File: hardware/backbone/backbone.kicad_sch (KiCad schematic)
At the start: 87 parts, among them J10 CORE_A, J11 MOUNT, J13 FIELD_B, J14 FIELD_A, J2 FROM_PREVIOUS, J4 FROM_PREVIOUS, J5 CONN_A, J7 CONN_B, J8 CORE_B, J9 TO NEXT, Q2 AO3401A, U11 470nH DCR=450m, U13 470nH DCR=450m, U15 ST25R100, U17 BLM18PG471SZ1D, U19 ESP32-S3-MINI-1, U2 SN65HVD230DR, U4 AP2112K-3.3TRG1, U8 G3VM-61VY3, X1 NX2016SA 27.12MHz

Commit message: New design, no NFC, added bottom-top side socket, board less expensive
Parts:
- removed ANT1, ANT2: Net-Tie-Width-0.50mm, SpaghettiLAB:ST25Rxxx-ANT-12x12mm, symbol STMICRO:root_1_Net-Tie-Width-0.50mm_STMICRO.SchLib
- removed C13, C16: 200pF 1%, SpaghettiLAB:C0603, symbol STMICRO:root_1_Capacitor 0402 240pF 50V 2% COG_STMICRO.SchLib
- removed C18, C20: 10pF, SpaghettiLAB:C0603, symbol STMICRO:root_1_Capacitor 0201 10pF 25V_STMICRO.SchLib
- removed C23: 100nF, SpaghettiLAB:C0603, symbol STMICRO:root_1_GRM033C71A104KE14D_STMICRO.SchLib
- removed C28, C32: 33pF 2%, SpaghettiLAB:C0603, symbol STMICRO:root_0_Capacitor 0603 39pF 50V 2% COG_STMICRO.SchLib
- removed C30, C35, C37, C58, C63, C65: 10nF, SpaghettiLAB:C0603, symbol STMICRO:root_1_GRM033R61E103KA12D_STMICRO.SchLib
- removed C33, C39, C41, C70: 2.2uF/10V, SpaghettiLAB:C0603, symbol STMICRO:root_1_GRM033R61A225ME47_STMICRO.SchLib
- removed C43, C55: 220pF, SpaghettiLAB:C0603, symbol STMICRO:root_1_Capacitor 0603 220pF 50V C0G 2%_STMICRO.SchLib
- removed C46, C54: 10pF, SpaghettiLAB:C0603, symbol STMICRO:root_1_Capacitor 0603 10pF 25V 5% C0G_STMICRO.SchLib
- removed C48, C51: 150pF, SpaghettiLAB:C0603, symbol STMICRO:root_1_Capacitor 0603 150pF 50V 2% COG_STMICRO.SchLib
- removed C60, C72: 1uF/10V, SpaghettiLAB:C0603, symbol STMICRO:root_1_GRM033R61A105ME15_STMICRO.SchLib
- removed C62: 4.7uF/10V, SpaghettiLAB:C0603, symbol STMICRO:root_1_GRM155R61A475MEAA_STMICRO.SchLib
- removed D2, D3: LED, SpaghettiLAB:LED0603-RD, symbol Device:LED
- removed J10: CORE_A, Connector_PinSocket_2.54mm:PinSocket_1x03_P2.54mm_Vertical, symbol Connector:Conn_01x03_Pin
- removed J11: MOUNT, Connector_PinHeader_2.54mm:PinHeader_1x05_P2.54mm_Horizontal, symbol Connector:Conn_01x05_Pin
- removed J13: FIELD_B, Connector_PinSocket_2.54mm:PinSocket_1x03_P2.54mm_Vertical, symbol Connector:Conn_01x03_Pin
- removed J14: FIELD_A, Connector_PinSocket_2.54mm:PinSocket_1x03_P2.54mm_Vertical, symbol Connector:Conn_01x03_Pin
- removed J4: FROM_PREVIOUS, Connector_PinSocket_2.54mm:PinSocket_1x05_P2.54mm_Horizontal, symbol Connector:Conn_01x05_Socket
- removed J5: CONN_A, Connector_PinSocket_2.54mm:PinSocket_1x03_P2.54mm_Vertical, symbol Connector:Conn_01x03_Pin
- removed J7: CONN_B, Connector_PinSocket_2.54mm:PinSocket_1x03_P2.54mm_Vertical, symbol Connector:Conn_01x03_Pin
- removed J8: CORE_B, Connector_PinSocket_2.54mm:PinSocket_1x03_P2.54mm_Vertical, symbol Connector:Conn_01x03_Pin
- removed L2: 420nH DCR=450m, STMICRO.PcbLib:COILCRAFT-SELF-SERIE-0402DF, symbol STMICRO:root_0_COILCRAFT-SELF-0402DF-421XJR_STMICRO.SchLib
- removed L4: BLM15PD121SN1D, symbol STMICRO:root_0_BLM15PD121SN1D_STMICRO.SchLib
- removed R11, R14: 1R5, SpaghettiLAB:R0603, symbol STMICRO:root_0_Resistor 0603 1R5 1%_STMICRO.SchLib
- removed R21, R22: 330R, SpaghettiLAB:R0603, symbol Device:R
- removed TP17, TP20: SMD/0.8mm, TestPoint:TestPoint_Pad_D1.0mm, symbol STMICRO:root_0_PLAGE-CMS-DIAM-0.8mm_STMICRO.SchLib
- removed TP2, TP4: SMD/0.8mm, TestPoint:TestPoint_Pad_D1.0mm, symbol STMICRO:root_1_PLAGE-CMS-DIAM-0.8mm_STMICRO.SchLib
- removed U11, U13: 470nH DCR=450m, SpaghettiLAB:IND-SMD_L1.6-W0.8-1, symbol SpaghettiLAB:LQW18CNR47J00D
- removed U15: ST25R100, SpaghettiLAB:QFN-24_L4.0-W4.0-P0.50-TL-EP2.8, symbol STMICRO:root_0_ST25R200_STMICRO.SchLib
- removed U17: BLM18PG471SZ1D, SpaghettiLAB:L0603, symbol SpaghettiLAB:BLM18PG471SZ1D
- removed X1: NX2016SA 27.12MHz, SpaghettiLAB:CRYSTAL-SMD_4P-L2.0-W1.6-BL, symbol STMICRO:root_1_NDK-NX2016SA-27.12MHZ-EXS00A-CS01188_STMICRO.SchLib_0
- added H1, H2, H3, H4: MountingHole, MountingHole:MountingHole_2.2mm_M2_DIN965, symbol Mechanical:MountingHole
- added J1, J140, J3: M20-7810645R, SpaghettiLAB:HARWIN_M20-7810645R, symbol SpaghettiLAB:M20-7810645R
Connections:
- net IO11 is gone; now on net STATUS: U19.15 (IO11)
- net IO7 is gone; now on net A0: U19.11 (IO7)
- net IO8 is gone; now on net A1: U19.12 (IO8)
- net IO9 is gone; now on net A2: U19.13 (IO9)
- net 5V: now also J3.2
- net A0: now also J3.6; no longer U19.34 (IO38)
- net A1: now also J3.8; no longer U19.33 (IO37)
- net A2: now also J3.10; no longer U19.32 (IO36)
- net A3: now also U19.14 (IO10), J3.12; no longer U19.31 (IO35)
- net GND: now also J3.3, J3.4
- net STATUS: no longer U19.14 (IO10)
- net VCORE: now also J3.1
- net IO12 renamed A4
- net A4: now also J3.11
- net IO13 renamed A5
- net A5: now also J3.9
- net IO14 renamed A6
- net A6: now also J3.7
- net IO15 renamed A7
- net A7: now also J3.5
- net NFC_CS renamed IO2
- net NFC_IRQ renamed IO5
- net NFC_MISO renamed IO6
- net NFC_MOSI renamed IO3
- net NFC_RST renamed IO1
- net NFC_SCK renamed IO4
- new net: J1.2, J140.1
- new net: J1.9, J140.10
- new net: J1.12, J140.11
- new net: J1.11, J140.12
- new net: J1.1, J140.2
- new net: J1.4, J140.3
- new net: J1.3, J140.4
- new net: J1.6, J140.5
- new net: J1.5, J140.6
- new net: J1.8, J140.7
- new net: J1.7, J140.8
- new net: J1.10, J140.9
- new net IO35: U19.31 (IO35)
- new net IO36: U19.32 (IO36)
- new net IO37: U19.33 (IO37)
- new net IO38: U19.34 (IO38)
- no-connect marks 22 -> 12
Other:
- note removed: "0402 NOT EASY TO FIND/MOUNT SWITCHED TO 0603, A RE-TUNE MAY BE NECESSARY"
- note removed: "0603"
- note removed: "0603 BETTER C0G/NP0"
- note removed: "BLM15PD121SN1D WAS NOT IN INVENTORY BUT IS THE SUGGESTED ONE"
- note removed: "NFC ANTENNA"
- note removed: "NFC ANTENNA PARAMETERS Type: PCB Spiral Coil (Double Layer) Frequency: 13.56 MHz Size: 12 mm x 12 mm Layers: TOP + BOTTOM copper Turns: 6 total (3 TOP + 3 BOTTOM) Connection: Series through vias PCB: Substrate: FR-4 Thickness: 1.6 mm Relative Er: 4.4 Copper thickness: 35 um Geometry: Track width: 0.5 mm Track spacing: 0.5 mm Outer diameter: 12 mm Inner diameter: 6 mm Average diameter: 9 mm Electr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"
- note removed: "NFC MODULE READER 0"
- note removed: "USED 0603 INSTEAD TO MATCH OTHER COMPONENTS OF THE NET"
- note removed: "| ADC | Channels | GPIO | | ADC1 | CH0-CH9 | **GPIO1-GPIO10** | | ADC2 | CH0-CH9 | **GPIO11-GPIO20** | NEXT REVIEW NEEDS THIS MODS"
- moved on the sheet: D5, R24

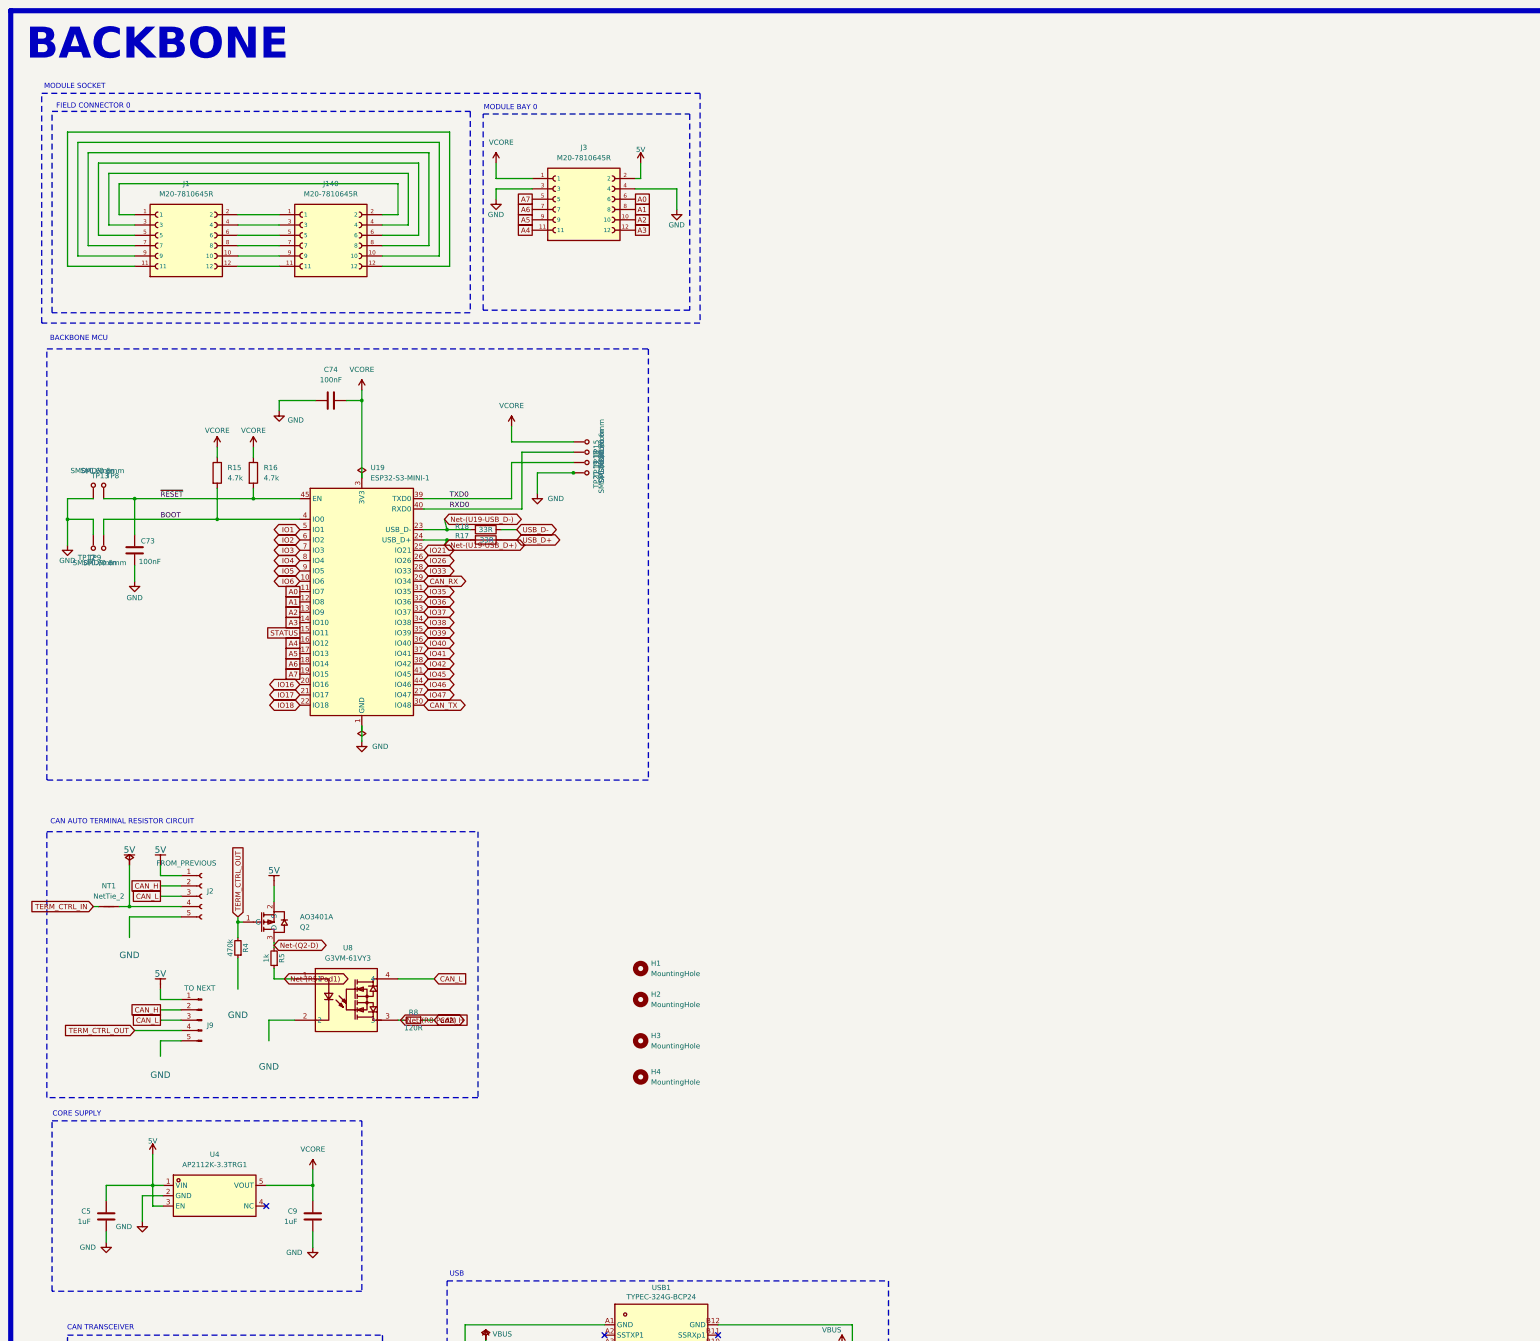
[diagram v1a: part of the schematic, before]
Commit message: Prepare V3 hardware with S3 FlexyPin socket and expansion connector libraries
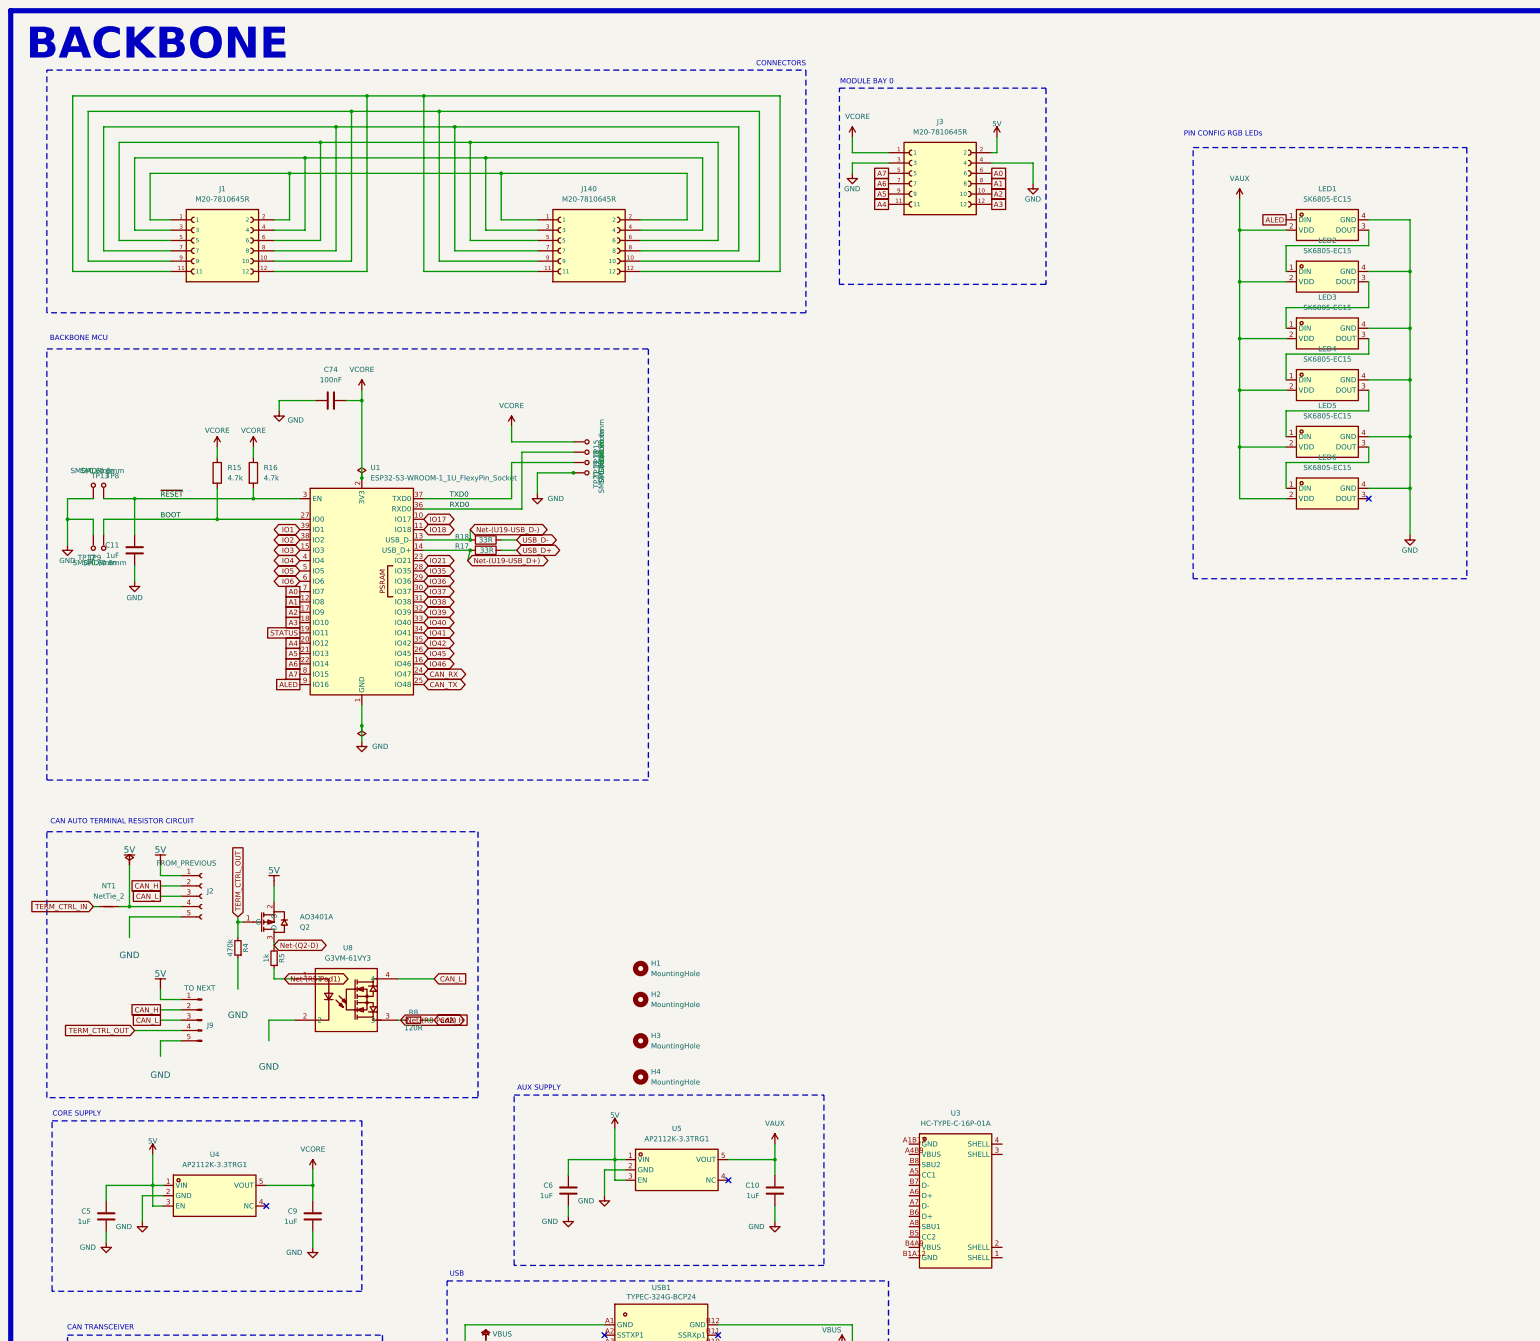
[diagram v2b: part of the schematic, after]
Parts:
- removed C73: 100nF, SpaghettiLAB:C0603, symbol Device:C
- removed U19: ESP32-S3-MINI-1, RF_Module:ESP32-S2-MINI-1, symbol RF_Module:ESP32-S3-MINI-1
- added C10, C11, C6: 1uF, SpaghettiLAB:C0603, symbol Device:C
- added LED1, LED2, LED3, LED4, LED5, LED6: SK6805-EC15, SpaghettiLABold:LED-SMD_4P-L1.5-W1.5-BL, symbol SpaghettiLABold:SK6805-EC15
- added U1: ESP32-S3-WROOM-1_1U_FlexyPin_Socket, FlexyPin:ESP32-S3-WROOM-1_1U_FlexyPin_Socket, symbol SpaghettiLab_FlexyPin:ESP32-S3-WROOM-1_1U_FlexyPin_Socket
- added U3: HC-TYPE-C-16P-01A, SpaghettiLAB:USB-C-SMD_HC-TYPE-C-16P-01A, symbol SpaghettiLABold:HC-TYPE-C-16P-01A
- added U5: AP2112K-3.3TRG1, SpaghettiLAB:SOT-25-5_L2.9-W1.6-P0.95-LS2.8-BL, symbol SpaghettiLab:AP2112K-3.3TRG1
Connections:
- net 5V: now also C6.2, U5.1 (VIN), U5.3 (EN)
- net A0: now also U1.7 (IO7)
- net A1: now also U1.12 (IO8)
- net A2: now also U1.17 (IO9)
- net A3: now also U1.18 (IO10)
- net A4: now also U1.20 (IO12)
- net A5: now also U1.21 (IO13)
- net A6: now also U1.22 (IO14)
- net A7: now also U1.8 (IO15)
- net BOOT: now also U1.27 (IO0)
- net CAN_RX: now also U1.24 (IO47)
- net CAN_TX: now also U1.25 (IO48)
- net GND: now also C10.1, C11.1, C6.1, LED1.4 (GND), LED2.4 (GND), LED3.4 (GND), LED4.4 (GND), LED5.4 (GND), LED6.4 (GND), U1.1 (GND), U1.40 (GND), U5.2 (GND)
- net IO1: now also U1.39 (IO1)
- net IO17: now also U1.10 (IO17)
- net IO18: now also U1.11 (IO18)
- net IO2: now also U1.38 (IO2)
- net IO21: now also U1.23 (IO21)
- net IO3: now also U1.15 (IO3)
- net IO35: now also U1.28 (IO35)
- net IO36: now also U1.29 (IO36)
- net IO37: now also U1.30 (IO37)
- net IO38: now also U1.31 (IO38)
- net IO39: now also U1.32 (IO39)
- net IO4: now also U1.4 (IO4)
- net IO40: now also U1.33 (IO40)
- net IO41: now also U1.34 (IO41)
- net IO42: now also U1.35 (IO42)
- net IO45: now also U1.26 (IO45)
- net IO46: now also U1.16 (IO46)
- net IO5: now also U1.5 (IO5)
- net IO6: now also U1.6 (IO6)
- net Net-(U19-USB_D+): now also U1.14 (USB_D+)
- net Net-(U19-USB_D-): now also U1.13 (USB_D-)
- net RXD0: now also U1.36 (RXD0)
- net STATUS: now also U1.19 (IO11)
- net TXD0: now also U1.37 (TXD0)
- net VCORE: now also U1.2 (3V3)
- net ~{RESET}: now also C11.2, U1.3 (EN)
- net at J1.2, J140.1: now also J1.1, J140.2
- net at J1.9, J140.10: now also J1.10, J140.9
- net at J1.12, J140.11: now also J1.11, J140.12
- net at J1.4, J140.3: now also J1.3, J140.4
- net at J1.6, J140.5: now also J1.5, J140.6
- net at J1.8, J140.7: now also J1.7, J140.8
- new net: LED1.3 (DOUT), LED2.1 (DIN)
- new net: LED2.3 (DOUT), LED3.1 (DIN)
- new net: LED3.3 (DOUT), LED4.1 (DIN)
- new net: LED4.3 (DOUT), LED5.1 (DIN)
- new net: LED5.3 (DOUT), LED6.1 (DIN)
- new net ALED: LED1.1 (DIN), U1.9 (IO16)
- new net VAUX: C10.2, LED1.2 (VDD), LED2.2 (VDD), LED3.2 (VDD), LED4.2 (VDD), LED5.2 (VDD), LED6.2 (VDD), U5.5 (VOUT)
- no-connect marks 12 -> 14
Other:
- note added: "AUX SUPPLY"
- note added: "CONNECTORS"
- note added: "PIN CONFIG RGB LEDs"
- note removed: "FIELD CONNECTOR 0"
- note removed: "MODULE SOCKET"
- moved on the sheet: J1, J140, J3, R17, R18
